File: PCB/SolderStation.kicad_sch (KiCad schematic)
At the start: 44 parts, among them J1 T12 TIP, J10 Aviation-GX12-6, J11 NTC, J2 DC IN, J3 ISP, J4 I2C, J5 Handset detect, J6 ENCODER, J7 OPTO, J8 LCD0802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

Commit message: Add files via upload
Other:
- note added: "A3 set to HIGH to power up IR LEDs"
- note removed: "A7 set to HIGH to power up IR LEDs"
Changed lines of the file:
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@@
     (effects (font (size 2.5908 2.5908) (thickness 0.5182) bold) (justify left bottom))
   )
-  (text "A7 set to HIGH to power up IR LEDs" (at 36.83 111.125 0)
+  (text "A3 set to HIGH to power up IR LEDs" (at 36.83 111.125 0)
     (effects (font (size 1.27 1.27)) (justify left bottom))
   )

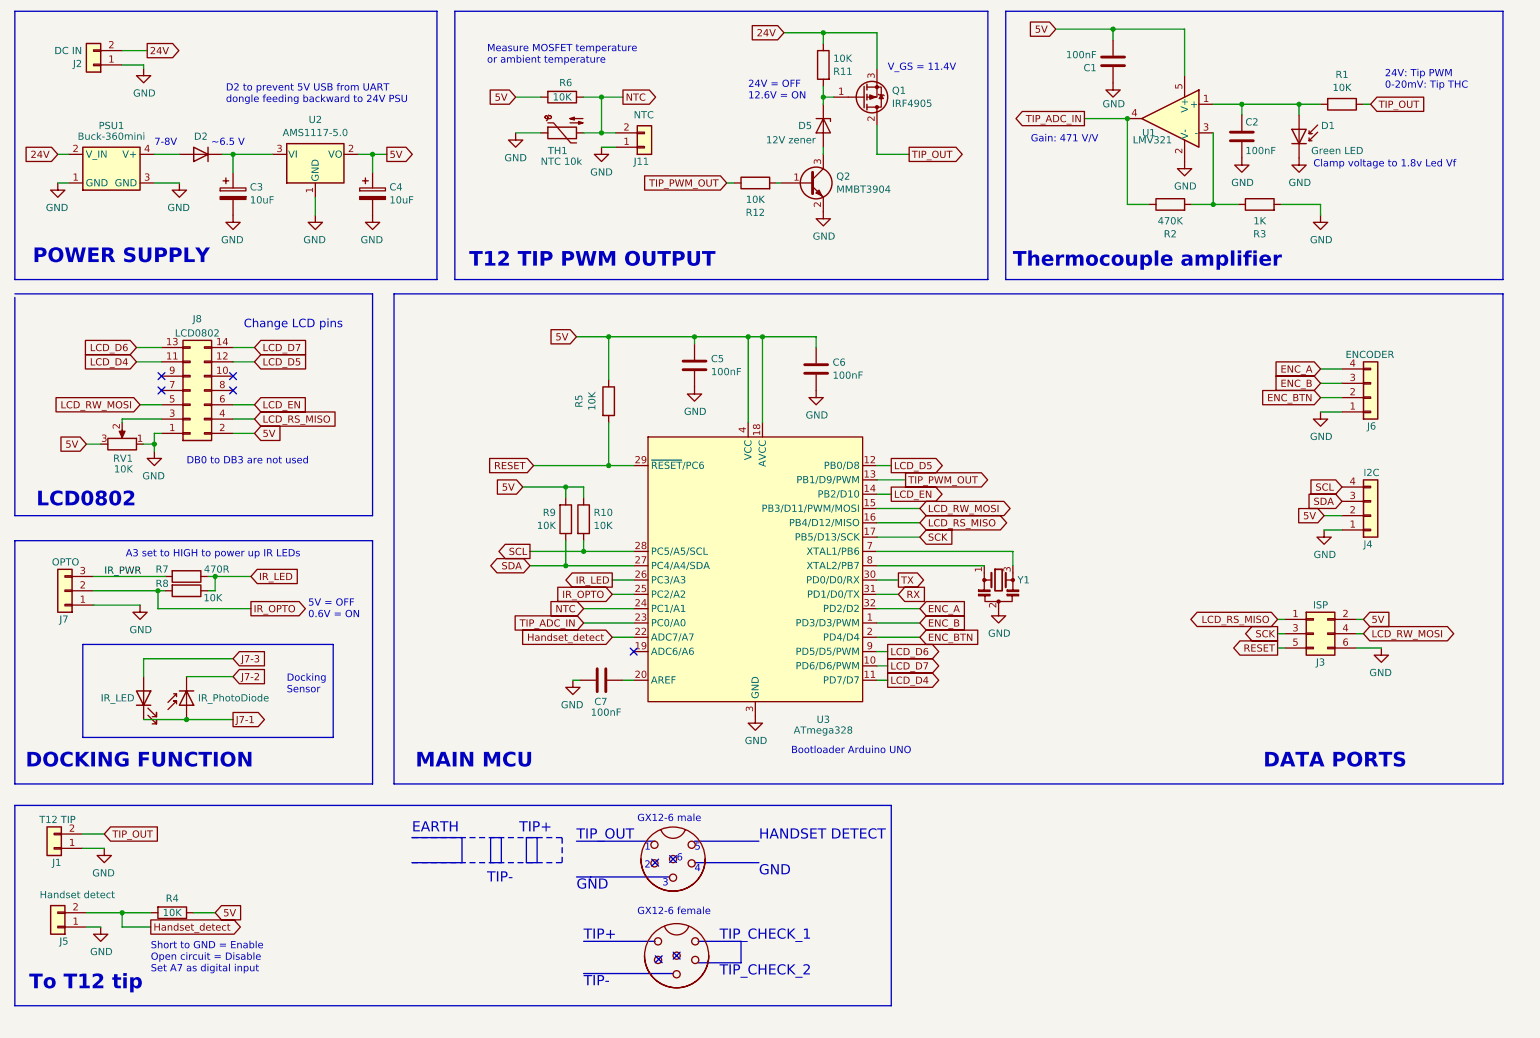
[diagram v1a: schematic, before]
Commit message: Add files via upload
- Upgrade project to Kicad 7.0
- Improve schematic details
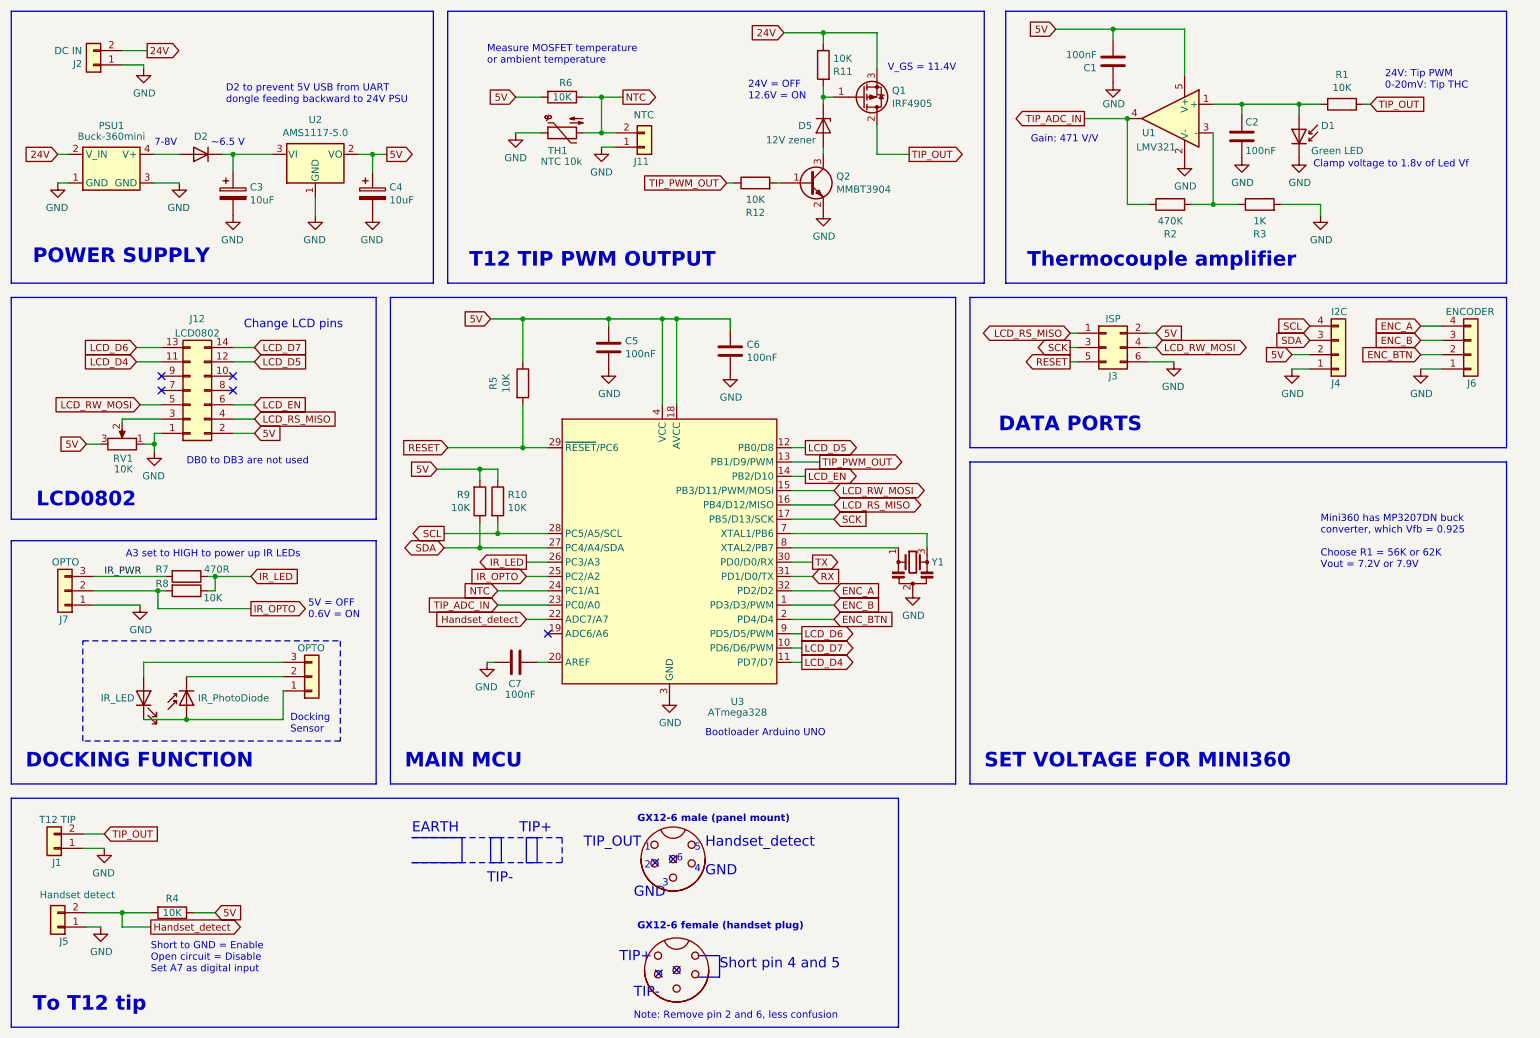
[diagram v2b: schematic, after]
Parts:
- added J8: OPTO, Connector_JST:JST_XH_B3B-XH-A_1x03_P2.50mm_Vertical, symbol Connector_Generic:Conn_01x03
- D3, D4, J1, J10, J11, J2, J3, J4, J5, J6, J7, J9: now left out of the parts list
- renumbered J8 to J12
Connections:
- net J7-1: no longer names the net of D3.1 (K), D4.2 (A)
- net J7-1: now also J8.1 (Pin_1)
- net J7-2: no longer names the net of D4.1 (K)
- net J7-2: now also J8.2 (Pin_2)
- net J7-3: no longer names the net of D3.2 (A)
- net J7-3: now also J8.3 (Pin_3)
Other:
- note added: "Clamp voltage to 1.8v of Led Vf"
- note added: "GX12-6 female (handset plug)"
- note added: "GX12-6 male (panel mount)"
- note added: "Handset_detect"
- note added: "Mini360 has MP3207DN buck converter, which Vfb = 0.925 Choose R1 = 56K or 62K Vout = 7.2V or 7.9V"
- note added: "Note: Remove pin 2 and 6, less confusion"
- note added: "SET VOLTAGE FOR MINI360"
- note added: "Short pin 4 and 5"
- note removed: "Clamp voltage to 1.8v Led Vf"
- note removed: "GX12-6 female"
- note removed: "GX12-6 male"
- note removed: "HANDSET DETECT"
- note removed: "TIP_CHECK_1"
- note removed: "TIP_CHECK_2"
- company: ceezblog.info -> ceezblog.info (2008 - 2022)
- title: T12 Solder Station r1.2 -> T12 Solder Station r0.5
- moved on the sheet: C5, C6, C7, J3, J4, J6, R10, R5, R9, U3, Y1
